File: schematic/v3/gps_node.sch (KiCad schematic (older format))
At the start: 69 parts, among them IC1 MCP73831/2, J1 Mounting Hole, J11 AVR ICSP, J12 UART RF, J13 LIPO_BAT, J14 SOLAR, J15 UART GPS, J16 FW_UPDATE, J17 u.FL connector, J2 Mounting Hole, J3 Mounting Hole, J4 Mounting Hole, J5 TEST Vbatt, J6 USB_OTG, J7 Test 3.3v, J8 Test Gnd, J9 Test V_bak, SW1 RS stock no. 448-0747, SW2 RESET, SW3 MODE, U1 TLV71333PDBV, U2 ublox-cam-m8q-0, U3 TLV71333PDBV, U4 ATMEGA32U4-AU, U5 RN2483, Y1 16MHz

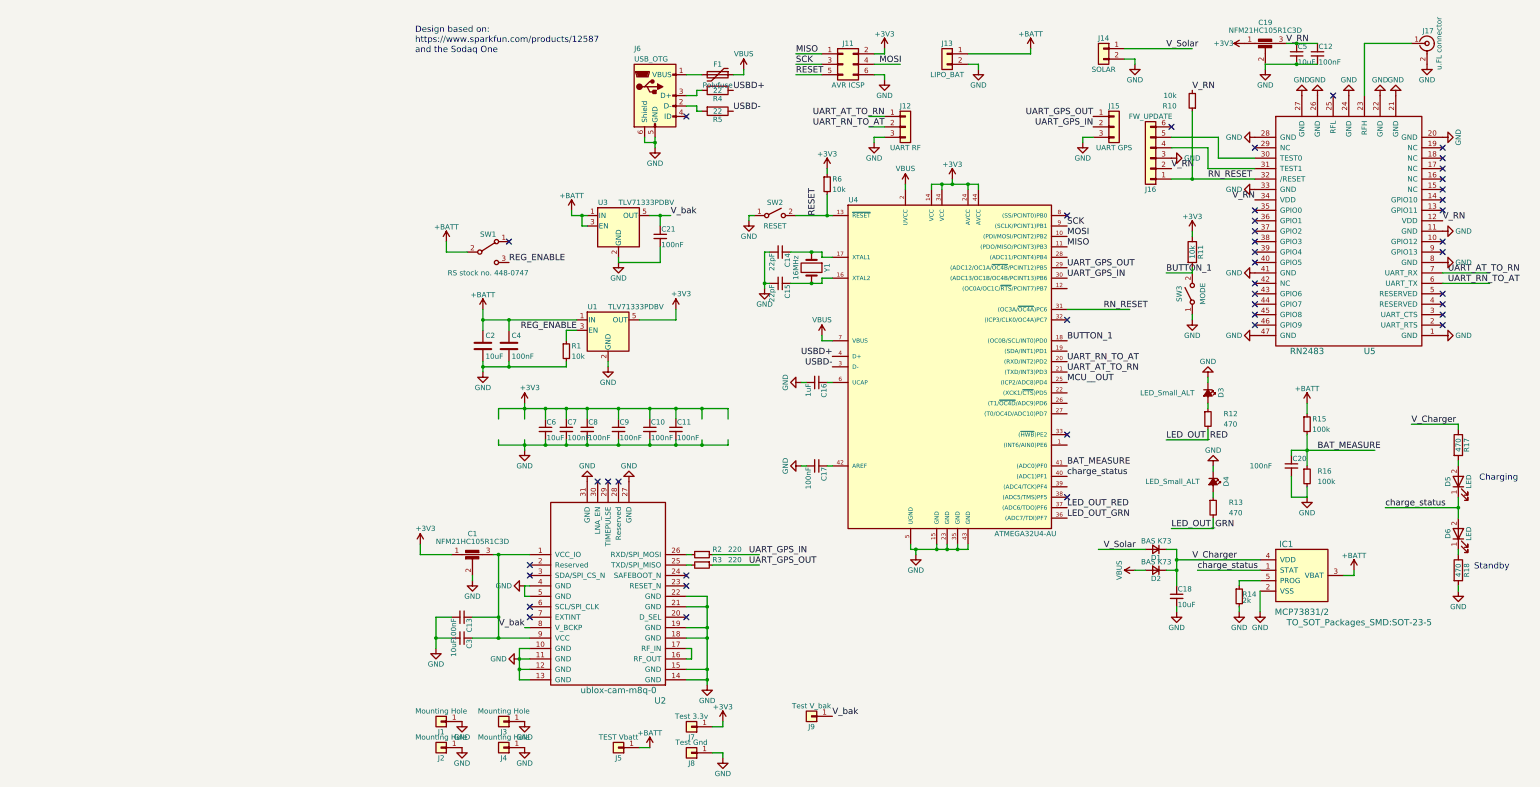
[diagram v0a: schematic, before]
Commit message: Updated d3 schematic to multiple sheets
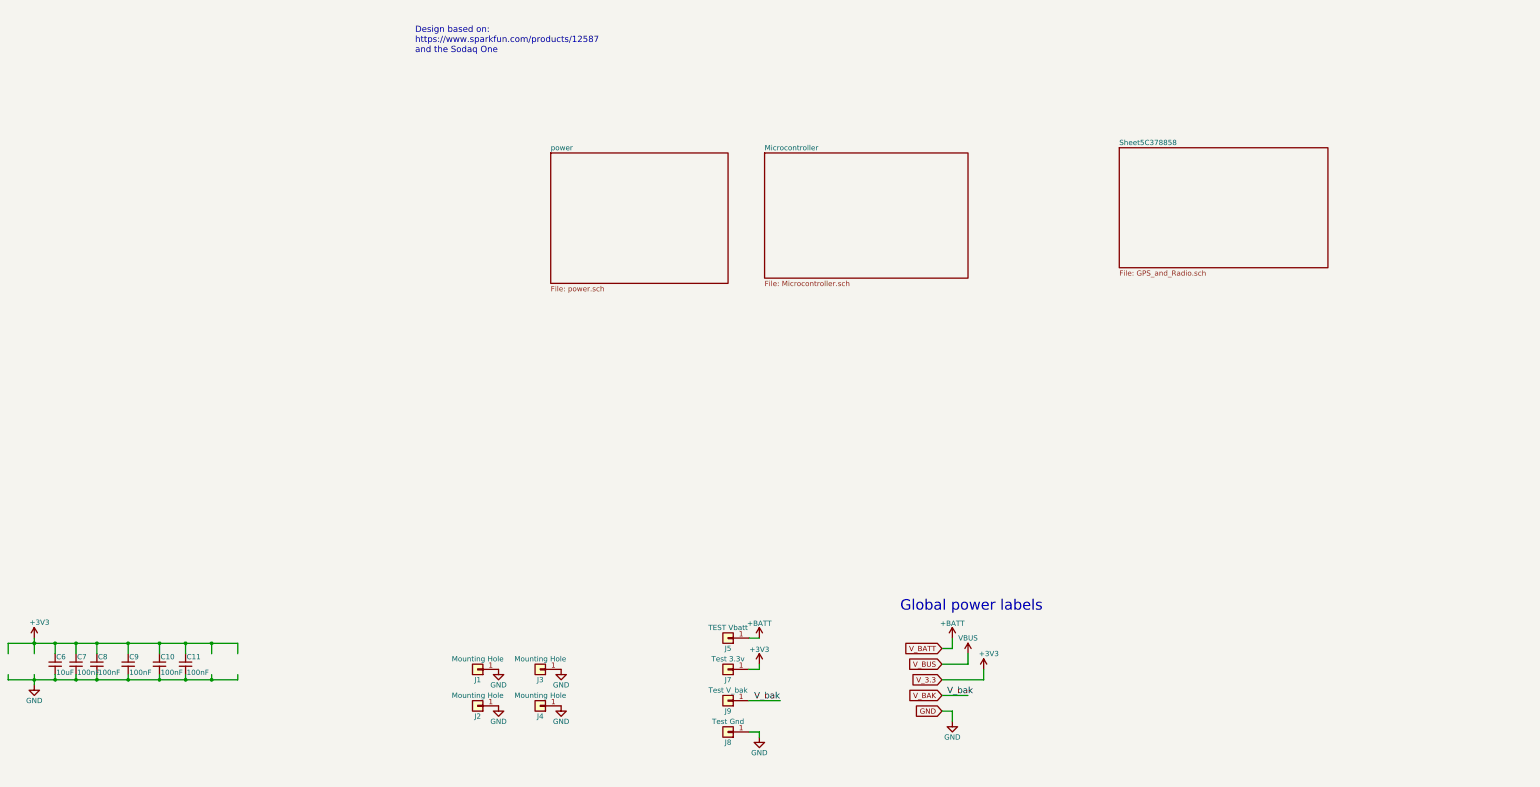
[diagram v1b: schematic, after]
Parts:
- removed C1, C19: NFM21HC105R1C3D, gps_node_components:C_FEEDTHROUGH_0805, symbol gps_node-rescue:C_Feedthrough
- removed C12, C13, C17, C20, C21: 100nF, Capacitors_SMD:C_0805, symbol gps_node-rescue:C_Small
- removed C14, C15: 22pF, Capacitors_SMD:C_0805, symbol gps_node-rescue:C_Small
- removed C16: 1uF, Capacitors_SMD:C_0805, symbol gps_node-rescue:C_Small
- removed C18, C3, C5: 10uF, Capacitors_SMD:C_0805, symbol gps_node-rescue:C_Small
- removed C2: 10uF, Capacitors_SMD:C_1206, symbol gps_node-rescue:C
- removed C4: 100nF, Capacitors_SMD:C_0805, symbol gps_node-rescue:C
- removed D1, D2: BAS K73, Diodes_SMD:D_SOT-23_ANK, symbol gps_node-rescue:D_Small
- removed D3, D4: LED_Small_ALT, LEDs:LED_0805, symbol gps_node-rescue:LED_Small_ALT
- removed D5, D6: LED, LEDs:LED_0805, symbol gps_node-rescue:LED
- removed F1: Polyfuse, gps_node_components:bourns polyfuse, symbol gps_node-rescue:Polyfuse
- removed IC1: MCP73831/2, TO_SOT_Packages_SMD:SOT-23-5, symbol gps_node-rescue:MCP73831_2
- removed J11: AVR ICSP, Pin_Headers:Pin_Header_Straight_2x03_Pitch2.54mm, symbol gps_node-rescue:Conn_02x03_Odd_Even
- removed J12: UART RF, Pin_Headers:Pin_Header_Straight_1x03_Pitch2.54mm, symbol gps_node-rescue:Conn_01x03
- removed J13: LIPO_BAT, Connectors_Molex:Molex_PicoBlade_53047-0210_02x1.25mm_Straight, symbol gps_node-rescue:Conn_01x02
- removed J14: SOLAR, Connectors_Molex:Molex_PicoBlade_53047-0210_02x1.25mm_Straight, symbol gps_node-rescue:Conn_01x02
- removed J15: UART GPS, Pin_Headers:Pin_Header_Straight_1x03_Pitch2.54mm, symbol gps_node-rescue:Conn_01x03
- removed J16: FW_UPDATE, Pin_Headers:Pin_Header_Straight_1x06_Pitch2.54mm, symbol gps_node-rescue:Conn_01x06
- removed J17: u.FL connector, gps_node_components:CONN-RF-UFL, symbol gps_node-rescue:Conn_Coaxial
- removed J6: USB_OTG, gps_node_components:Molex_Microusb, symbol gps_node-rescue:USB_OTG
- removed R1, R10, R6: 10k, Resistors_SMD:R_0805, symbol gps_node-rescue:R_Small
- removed R11: 10k, Resistors_SMD:R_0805, symbol gps_node-rescue:R
- removed R12, R13: 470, Resistors_SMD:R_0805, symbol gps_node-rescue:R_Small
- removed R14: 2k, Resistors_SMD:R_0805, symbol gps_node-rescue:R_Small
- removed R15, R16: 100k, Resistors_SMD:R_0805, symbol gps_node-rescue:R_Small
- removed R17, R18: 470, Resistors_SMD:R_0805, symbol gps_node-rescue:R
- removed R2, R3: 220, Resistors_SMD:R_0805, symbol gps_node-rescue:R_Small
- removed R4, R5: 22, Resistors_SMD:R_0805, symbol gps_node-rescue:R
- removed SW1: RS stock no. 448-0747, Pin_Headers:Pin_Header_Straight_1x03_Pitch2.54mm, symbol gps_node-rescue:SW_SPDT
- removed SW2: RESET, Buttons_Switches_SMD:SW_SPST_PTS645, symbol gps_node-rescue:SW_SPST
- removed SW3: MODE, Buttons_Switches_SMD:SW_SPST_PTS645, symbol gps_node-rescue:SW_SPST
- removed U1, U3: TLV71333PDBV, TO_SOT_Packages_SMD:SOT-23-5, symbol gps_node-rescue:TLV71333PDBV
- removed U2: ublox-cam-m8q-0, drawn_by_jpmeijers:ublox-cam-m8q-0, symbol drawn_by_jpmeijers:ublox-cam-m8q-0
- removed U4: ATMEGA32U4-AU, Housings_QFP:TQFP-44_10x10mm_Pitch0.8mm, symbol gps_node-rescue:ATMEGA32U4-AU
- removed U5: RN2483, drawn_by_jpmeijers:RN2483, symbol drawn_by_jpmeijers:RN2483
- removed Y1: 16MHz, gps_node_components:QC3CA_16MHz, symbol gps_node-rescue:Crystal
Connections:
- net labels added: V_3.3, V_BAK, V_BATT, V_BUS
- net labels removed: BAT_MEASURE, BUTTON_1, LED_OUT_GRN, LED_OUT_RED, MCU__OUT, MISO, MOSI, REG_ENABLE, RESET, RN_RESET, SCK, UART_AT_TO_RN, UART_GPS_IN, UART_GPS_OUT, UART_RN_TO_AT, USBD+, USBD-, V_Charger, V_RN, V_Solar, charge_status
- wire segments 261 -> 55
- no-connect marks 43 -> 0
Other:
- note added: "Global power labels"
- note removed: "Charging"
- note removed: "Standby"
- moved on the sheet: C10, C11, C6, C7, C8, C9, J1, J2, J3, J4, J5, J7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

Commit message: Small cleanup
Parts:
- removed C10, C11, C7, C8, C9: 100nF, Capacitors_SMD:C_0805, symbol gps_node-rescue:C_Small
- removed C6: 10uF, Capacitors_SMD:C_0805, symbol gps_node-rescue:C_Small
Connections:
- wire segments 55 -> 21
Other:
- note added: "Mounting Holes"
- note added: "Power test pads"
- moved on the sheet: J1, J2, J3, J4, J5, J7, J8, J9

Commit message: Started PCB layout
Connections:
- net labels removed: V_bak
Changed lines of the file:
@@
 P 5500 4800
 AR Path="/5BFC4BE8/5C01CDE9" Ref="#PWR?"  Part="1"
-AR Path="/5C01CDE9" Ref="#PWR?"  Part="1"
-F 0 "#PWR?" H 5500 4650 50  0001 C CNN
+AR Path="/5C01CDE9" Ref="#PWR0101"  Part="1"
+F 0 "#PWR0101" H 5500 4650 50  0001 C CNN
 F 1 "+3V3" H 5550 4950 50  0000 C CNN
 F 2 "" H 5500 4800 50  0001 C CNN
@@
 P 5200 5300
 AR Path="/5BFC4BE8/5C01CDF4" Ref="#PWR?"  Part="1"
-AR Path="/5C01CDF4" Ref="#PWR?"  Part="1"
-F 0 "#PWR?" H 5200 5050 50  0001 C CNN
+AR Path="/5C01CDF4" Ref="#PWR0102"  Part="1"
+F 0 "#PWR0102" H 5200 5050 50  0001 C CNN
 F 1 "GND" H 5200 5150 50  0000 C CNN
 F 2 "" H 5200 5300 50  0001 C CNN
@@
 	5200 5200 5200 5300
 Text Label 5150 5050 0    60   ~ 0
-V_bak
+V_BAK
 $Comp
 L power:VBUS #PWR?
@@
 P 5350 4650
 AR Path="/5BFC4BE8/5C01CDFD" Ref="#PWR?"  Part="1"
-AR Path="/5C01CDFD" Ref="#PWR?"  Part="1"
-F 0 "#PWR?" H 5350 4500 50  0001 C CNN
+AR Path="/5C01CDFD" Ref="#PWR0103"  Part="1"
+F 0 "#PWR0103" H 5350 4500 50  0001 C CNN
 F 1 "VBUS" H 5350 4800 50  0000 C CNN
 F 2 "" H 5350 4650 50  0001 C CNN
@@
 P 5200 4500
 AR Path="/5BFC4BE8/5C01CE03" Ref="#PWR?"  Part="1"
-AR Path="/5C01CE03" Ref="#PWR?"  Part="1"
-F 0 "#PWR?" H 5200 4350 50  0001 C CNN
+AR Path="/5C01CE03" Ref="#PWR0104"  Part="1"
+F 0 "#PWR0104" H 5200 4350 50  0001 C CNN
 F 1 "+BATT" H 5200 4640 50  0000 C CNN
 F 2 "" H 5200 4500 50  0001 C CNN
@@
 Global power labels
 Text Label 2450 5250 0    60   ~ 0
-V_bak
+V_BAK
 Wire Wire Line
 	2400 5250 2700 5250

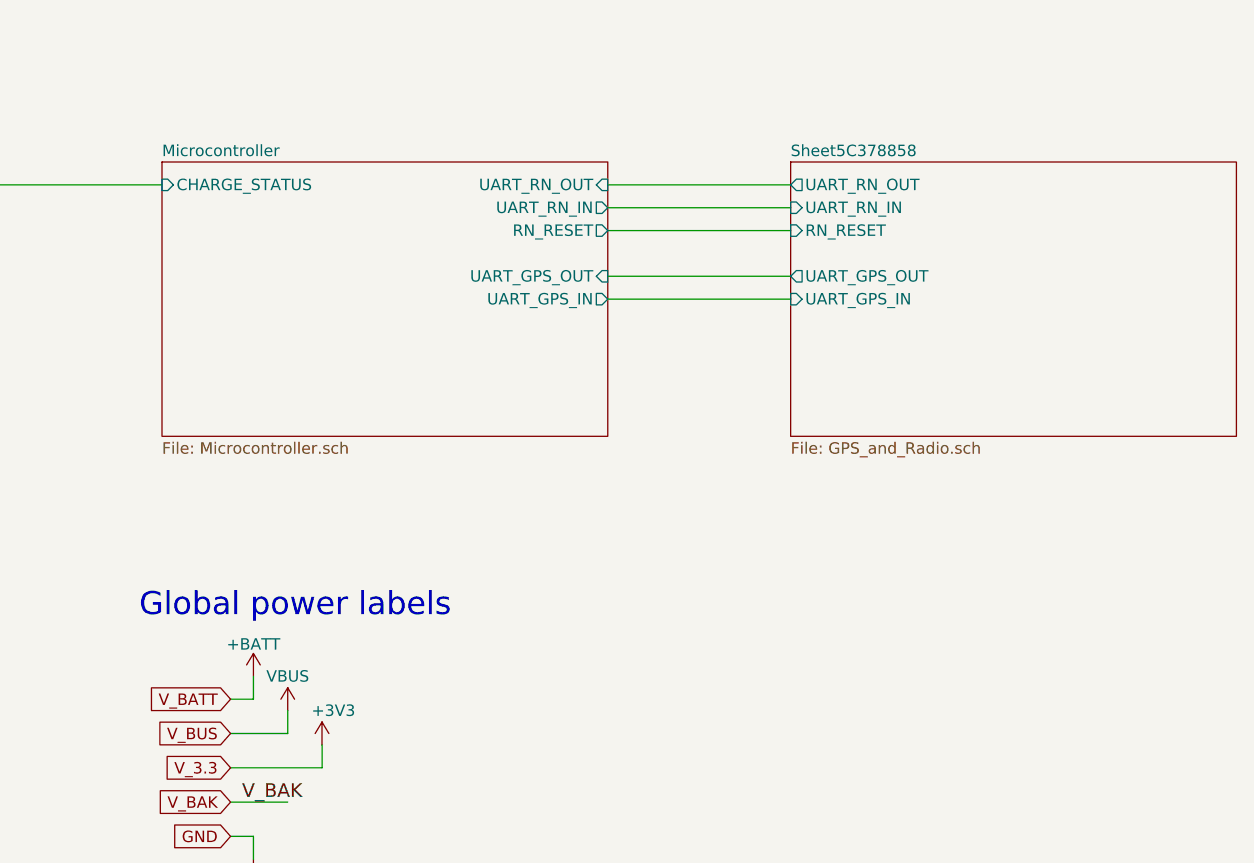
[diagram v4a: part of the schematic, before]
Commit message: Adds Accelerometer, layout almost done
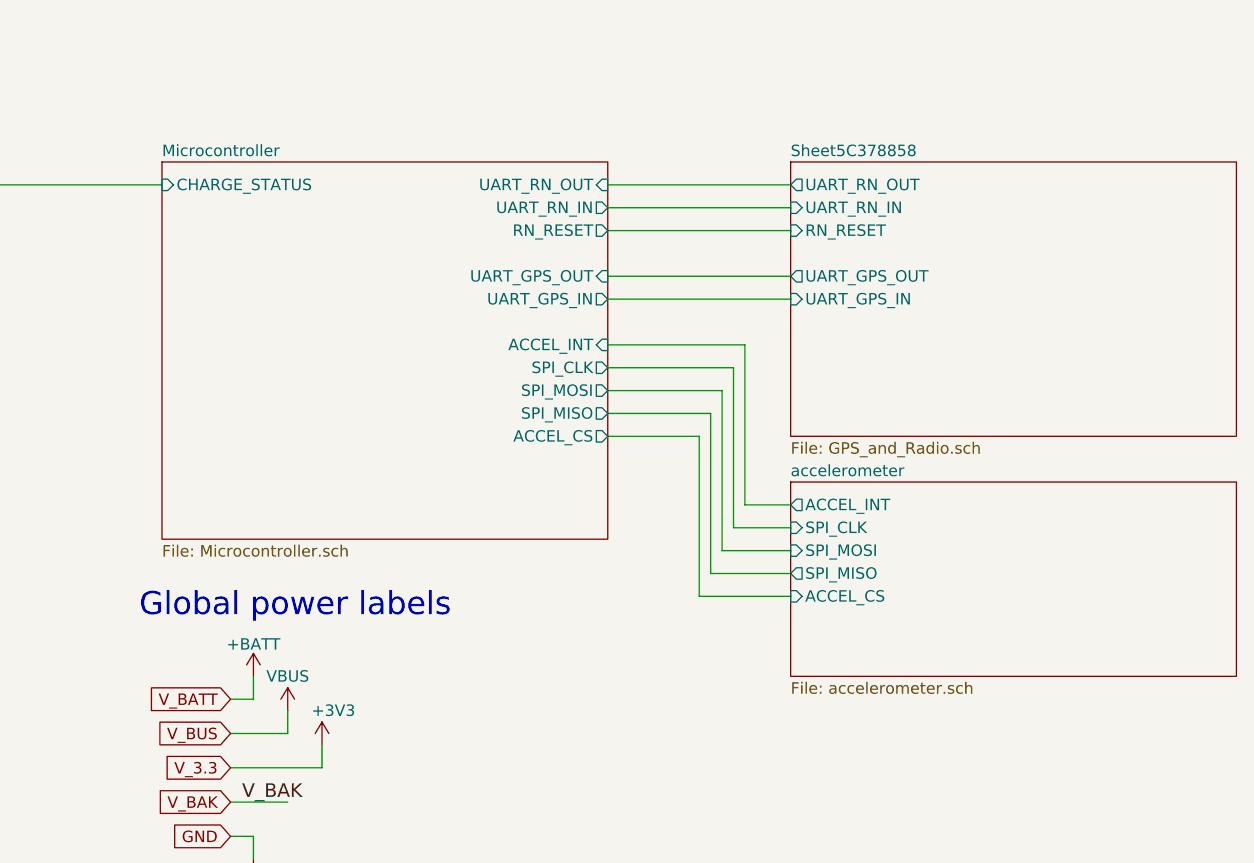
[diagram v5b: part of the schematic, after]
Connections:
- wire segments 21 -> 36
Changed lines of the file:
@@
 $Descr A4 11693 8268
 encoding utf-8
-Sheet 1 4
+Sheet 1 5
 Title ""
 Date ""
@@
 	2400 5250 2700 5250
 $Sheet
-S 4800 2250 1950 1200
+S 4800 2250 1950 1650
 U 5C0A9442
 F0 "Microcontroller" 50
@@
 F6 "UART_GPS_IN" O R 6750 2850 50
 F7 "CHARGE_STATUS" I L 4800 2350 50
+F8 "ACCEL_INT" I R 6750 3050 50
+F9 "SPI_MOSI" O R 6750 3250 50
+F10 "SPI_MISO" O R 6750 3350 50
+F11 "ACCEL_CS" O R 6750 3450 50
+F12 "SPI_CLK" O R 6750 3150 50
 $EndSheet
 $Sheet
@@
 Text Notes 2100 6250 0    101  ~ 0
 Mounting Holes
+$Sheet
+S 7550 3650 1950 850
+U 5BEAA40F
+F0 "accelerometer" 50
+F1 "accelerometer.sch" 50
+F2 "SPI_CLK" I L 7550 3850 50
+F3 "SPI_MOSI" I L 7550 3950 50
+F4 "SPI_MISO" O L 7550 4050 50
+F5 "ACCEL_CS" I L 7550 4150 50
+F6 "ACCEL_INT" O L 7550 3750 50
+$EndSheet
+Wire Wire Line
+	7550 3750 7350 3750
+Wire Wire Line
+	7350 3750 7350 3050
+Wire Wire Line
+	7350 3050 6750 3050
+Wire Wire Line
+	6750 3150 7300 3150
+Wire Wire Line
+	7300 3150 7300 3850
+Wire Wire Line
+	7300 3850 7550 3850
+Wire Wire Line
+	7550 3950 7250 3950
+Wire Wire Line
+	7250 3950 7250 3250
+Wire Wire Line
+	7250 3250 6750 3250
+Wire Wire Line
+	6750 3350 7200 3350
+Wire Wire Line
+	7200 3350 7200 4050
+Wire Wire Line
+	7200 4050 7550 4050
+Wire Wire Line
+	7550 4150 7150 4150
+Wire Wire Line
+	7150 4150 7150 3450
+Wire Wire Line
+	7150 3450 6750 3450
 $EndSCHEMATC

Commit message: Cleaned up schematic
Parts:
- J1, J2, J3, J4: footprint Mounting_Holes:MountingHole_3.2mm_M3_ISO14580_Pad -> MountingHole:MountingHole_3.2mm_M3_ISO14580_Pad
- J5, J7, J8, J9: footprint Socket_Strips:Socket_Strip_Straight_1x01_Pitch2.54mm -> Connector_PinHeader_2.54mm:PinHeader_1x01_P2.54mm_Vertical
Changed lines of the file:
@@
 F 0 "J1" H 2300 6800 50  0000 C CNN
 F 1 "Mounting Hole" H 2300 6600 50  0000 C CNN
-F 2 "Mounting_Holes:MountingHole_3.2mm_M3_ISO14580_Pad" H 2300 6700 50  0001 C CNN
+F 2 "MountingHole:MountingHole_3.2mm_M3_ISO14580_Pad" H 2300 6700 50  0001 C CNN
 F 3 "" H 2300 6700 50  0001 C CNN
 	1    2300 6700
@@
 F 0 "J2" H 2300 7150 50  0000 C CNN
 F 1 "Mounting Hole" H 2300 6950 50  0000 C CNN
-F 2 "Mounting_Holes:MountingHole_3.2mm_M3_ISO14580_Pad" H 2300 7050 50  0001 C CNN
+F 2 "MountingHole:MountingHole_3.2mm_M3_ISO14580_Pad" H 2300 7050 50  0001 C CNN
 F 3 "" H 2300 7050 50  0001 C CNN
 	1    2300 7050
@@
 F 0 "J3" H 2900 6800 50  0000 C CNN
 F 1 "Mounting Hole" H 2900 6600 50  0000 C CNN
-F 2 "Mounting_Holes:MountingHole_3.2mm_M3_ISO14580_Pad" H 2900 6700 50  0001 C CNN
+F 2 "MountingHole:MountingHole_3.2mm_M3_ISO14580_Pad" H 2900 6700 50  0001 C CNN
 F 3 "" H 2900 6700 50  0001 C CNN
 	1    2900 6700
@@
 F 0 "J4" H 2900 7150 50  0000 C CNN
 F 1 "Mounting Hole" H 2900 6950 50  0000 C CNN
-F 2 "Mounting_Holes:MountingHole_3.2mm_M3_ISO14580_Pad" H 2900 7050 50  0001 C CNN
+F 2 "MountingHole:MountingHole_3.2mm_M3_ISO14580_Pad" H 2900 7050 50  0001 C CNN
 F 3 "" H 2900 7050 50  0001 C CNN
 	1    2900 7050
@@
 F 0 "J5" H 2200 4750 50  0000 C CNN
 F 1 "TEST Vbatt" H 2200 4550 50  0000 C CNN
-F 2 "Socket_Strips:Socket_Strip_Straight_1x01_Pitch2.54mm" H 2200 4650 50  0001 C CNN
+F 2 "Connector_PinHeader_2.54mm:PinHeader_1x01_P2.54mm_Vertical" H 2200 4650 50  0001 C CNN
 F 3 "" H 2200 4650 50  0001 C CNN
 	1    2200 4650
@@
 F 0 "J7" H 2200 5050 50  0000 C CNN
 F 1 "Test 3.3v" H 2200 4850 50  0000 C CNN
-F 2 "Socket_Strips:Socket_Strip_Straight_1x01_Pitch2.54mm" H 2200 4950 50  0001 C CNN
+F 2 "Connector_PinHeader_2.54mm:PinHeader_1x01_P2.54mm_Vertical" H 2200 4950 50  0001 C CNN
 F 3 "" H 2200 4950 50  0001 C CNN
 	1    2200 4950
@@
 F 0 "J8" H 2200 5650 50  0000 C CNN
 F 1 "Test Gnd" H 2200 5450 50  0000 C CNN
-F 2 "Socket_Strips:Socket_Strip_Straight_1x01_Pitch2.54mm" H 2200 5550 50  0001 C CNN
+F 2 "Connector_PinHeader_2.54mm:PinHeader_1x01_P2.54mm_Vertical" H 2200 5550 50  0001 C CNN
 F 3 "" H 2200 5550 50  0001 C CNN
 	1    2200 5550
@@
 F 0 "J9" H 2200 5350 50  0000 C CNN
 F 1 "Test V_bak" H 2200 5150 50  0000 C CNN
-F 2 "Socket_Strips:Socket_Strip_Straight_1x01_Pitch2.54mm" H 2200 5250 50  0001 C CNN
+F 2 "Connector_PinHeader_2.54mm:PinHeader_1x01_P2.54mm_Vertical" H 2200 5250 50  0001 C CNN
 F 3 "" H 2200 5250 50  0001 C CNN
 	1    2200 5250
